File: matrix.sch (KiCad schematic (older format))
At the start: 285 parts, among them SW2 SW_SPDT, SW3 SW_SPDT

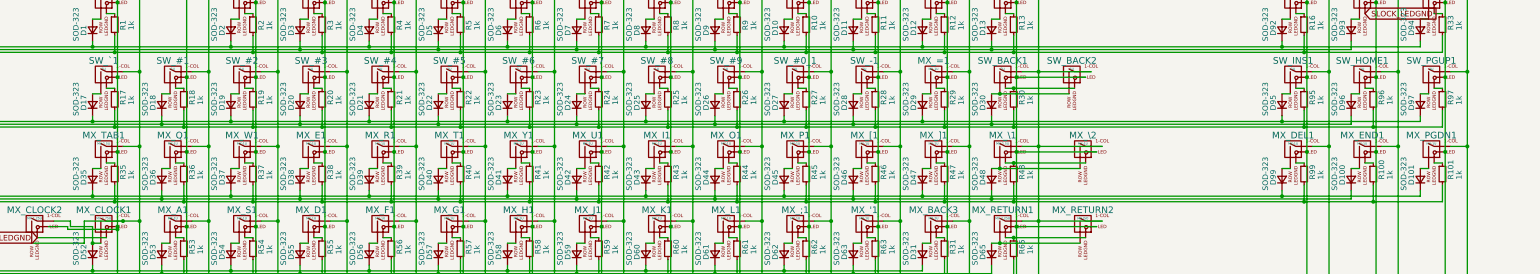
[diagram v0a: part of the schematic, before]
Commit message: Additional row footprint update
Update of a row of footprints from MX only to Alps compatible.
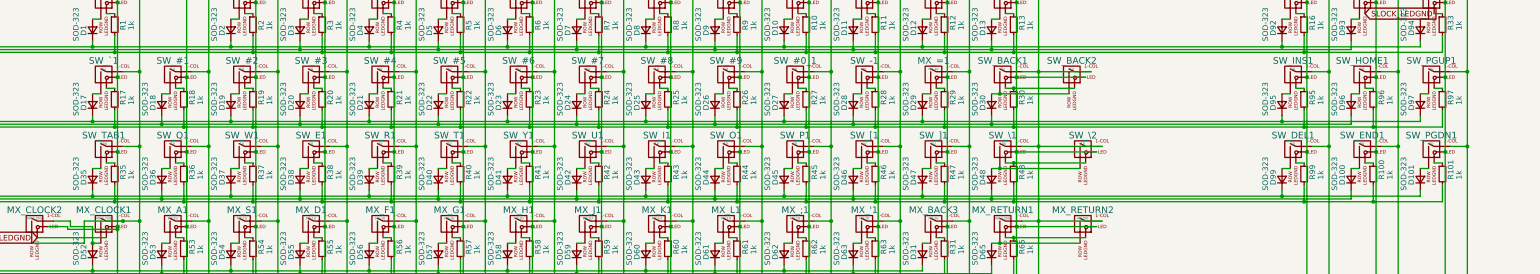
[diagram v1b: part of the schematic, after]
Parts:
- SW_DEL1: renamed from MX_DEL1; value MX-1U -> 1U; footprint MX_Alps_Hybrid:MXOnly-1U -> MX_Alps_Hybrid:MX-1U
- SW_E1: renamed from MX_E1; value MX-1U -> 1U; footprint MX_Alps_Hybrid:MXOnly-1U -> MX_Alps_Hybrid:MX-1U
- SW_END1: renamed from MX_END1; value MX-1U -> 1U; footprint MX_Alps_Hybrid:MXOnly-1U -> MX_Alps_Hybrid:MX-1U
- SW_I1: renamed from MX_I1; value MX-1U -> 1U; footprint MX_Alps_Hybrid:MXOnly-1U -> MX_Alps_Hybrid:MX-1U
- SW_O1: renamed from MX_O1; value MX-1U -> 1U; footprint MX_Alps_Hybrid:MXOnly-1U -> MX_Alps_Hybrid:MX-1U
- SW_P1: renamed from MX_P1; value MX-1U -> 1U; footprint MX_Alps_Hybrid:MXOnly-1U -> MX_Alps_Hybrid:MX-1U
- SW_PGDN1: renamed from MX_PGDN1; value MX-1U -> 1U; footprint MX_Alps_Hybrid:MXOnly-1U -> MX_Alps_Hybrid:MX-1U
- SW_Q1: renamed from MX_Q1; value MX-1U -> 1U; footprint MX_Alps_Hybrid:MXOnly-1U -> MX_Alps_Hybrid:MX-1U
- SW_R1: renamed from MX_R1; value MX-1U -> 1U; footprint MX_Alps_Hybrid:MXOnly-1U -> MX_Alps_Hybrid:MX-1U
- SW_T1: renamed from MX_T1; value MX-1U -> 1U; footprint MX_Alps_Hybrid:MXOnly-1U -> MX_Alps_Hybrid:MX-1U
- SW_TAB1: renamed from MX_TAB1; value MX-1.5U -> 1.5U; footprint MX_Alps_Hybrid:MXOnly-1.5U -> MX_Alps_Hybrid:MX-1.5U
- SW_U1: renamed from MX_U1; value MX-1U -> 1U; footprint MX_Alps_Hybrid:MXOnly-1U -> MX_Alps_Hybrid:MX-1U
- SW_W1: renamed from MX_W1; value MX-1U -> 1U; footprint MX_Alps_Hybrid:MXOnly-1U -> MX_Alps_Hybrid:MX-1U
- SW_Y1: renamed from MX_Y1; value MX-1U -> 1U; footprint MX_Alps_Hybrid:MXOnly-1U -> MX_Alps_Hybrid:MX-1U
- SW_[1: renamed from MX_[1; value MX-1U -> 1U; footprint MX_Alps_Hybrid:MXOnly-1U -> MX_Alps_Hybrid:MX-1U
- SW_\1: renamed from MX_\1; value MX-1.5U -> 1.5U; footprint MX_Alps_Hybrid:MXOnly-1.5U -> MX_Alps_Hybrid:MX-1.5U
- SW_\2: renamed from MX_\2; value MX-1U -> 1U; footprint MX_Alps_Hybrid:MXOnly-1U -> MX_Alps_Hybrid:MX-1U
- SW_]1: renamed from MX_]1; value MX-1U -> 1U; footprint MX_Alps_Hybrid:MXOnly-1U -> MX_Alps_Hybrid:MX-1U
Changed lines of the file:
@@
 $EndComp
 $Comp
-L MX_Alps_Hybrids:MX-1.5U MX_TAB1
+L MX_Alps_Hybrids:MX-1.5U SW_TAB1
 U 1 1 5A2ED339
 P 4825 4100
-F 0 "MX_TAB1" H 4825 4225 60  0000 C CNN
-F 1 "MX-1.5U" H 4825 4150 20  0000 C CNN
-F 2 "MX_Alps_Hybrid:MXOnly-1.5U" H 4800 4075 60  0001 C CNN
+F 0 "SW_TAB1" H 4825 4225 60  0000 C CNN
+F 1 "1.5U" H 4825 4150 20  0000 C CNN
+F 2 "MX_Alps_Hybrid:MX-1.5U" H 4800 4075 60  0001 C CNN
 F 3 "" H 4800 4075 60  0001 C CNN
 	1    4825 4100
@@
 $EndComp
 $Comp
-L MX_Alps_Hybrids:MX-1U MX_Q1
+L MX_Alps_Hybrids:MX-1U SW_Q1
 U 1 1 5A2ED361
 P 5450 4100
-F 0 "MX_Q1" H 5450 4225 60  0000 C CNN
-F 1 "MX-1U" H 5450 4150 20  0000 C CNN
-F 2 "MX_Alps_Hybrid:MXOnly-1U" H 5425 4075 60  0001 C CNN
+F 0 "SW_Q1" H 5450 4225 60  0000 C CNN
+F 1 "1U" H 5450 4150 20  0000 C CNN
+F 2 "MX_Alps_Hybrid:MX-1U" H 5425 4075 60  0001 C CNN
 F 3 "" H 5425 4075 60  0001 C CNN
 	1    5450 4100
@@
 $EndComp
 $Comp
-L MX_Alps_Hybrids:MX-1U MX_W1
+L MX_Alps_Hybrids:MX-1U SW_W1
 U 1 1 5A2ED375
 P 6075 4100
-F 0 "MX_W1" H 6075 4225 60  0000 C CNN
-F 1 "MX-1U" H 6075 4150 20  0000 C CNN
-F 2 "MX_Alps_Hybrid:MXOnly-1U" H 6050 4075 60  0001 C CNN
+F 0 "SW_W1" H 6075 4225 60  0000 C CNN
+F 1 "1U" H 6075 4150 20  0000 C CNN
+F 2 "MX_Alps_Hybrid:MX-1U" H 6050 4075 60  0001 C CNN
 F 3 "" H 6050 4075 60  0001 C CNN
 	1    6075 4100
@@
 $EndComp
 $Comp
-L MX_Alps_Hybrids:MX-1U MX_E1
+L MX_Alps_Hybrids:MX-1U SW_E1
 U 1 1 5A2ED389
 P 6700 4100
-F 0 "MX_E1" H 6700 4225 60  0000 C CNN
-F 1 "MX-1U" H 6700 4150 20  0000 C CNN
-F 2 "MX_Alps_Hybrid:MXOnly-1U" H 6675 4075 60  0001 C CNN
+F 0 "SW_E1" H 6700 4225 60  0000 C CNN
+F 1 "1U" H 6700 4150 20  0000 C CNN
+F 2 "MX_Alps_Hybrid:MX-1U" H 6675 4075 60  0001 C CNN
 F 3 "" H 6675 4075 60  0001 C CNN
 	1    6700 4100
@@
 $EndComp
 $Comp
-L MX_Alps_Hybrids:MX-1U MX_R1
+L MX_Alps_Hybrids:MX-1U SW_R1
 U 1 1 5A2ED39D
 P 7325 4100
-F 0 "MX_R1" H 7325 4225 60  0000 C CNN
-F 1 "MX-1U" H 7325 4150 20  0000 C CNN
-F 2 "MX_Alps_Hybrid:MXOnly-1U" H 7300 4075 60  0001 C CNN
+F 0 "SW_R1" H 7325 4225 60  0000 C CNN
+F 1 "1U" H 7325 4150 20  0000 C CNN
+F 2 "MX_Alps_Hybrid:MX-1U" H 7300 4075 60  0001 C CNN
 F 3 "" H 7300 4075 60  0001 C CNN
 	1    7325 4100
@@
 $EndComp
 $Comp
-L MX_Alps_Hybrids:MX-1U MX_T1
+L MX_Alps_Hybrids:MX-1U SW_T1
 U 1 1 5A2ED3B1
 P 7950 4100
-F 0 "MX_T1" H 7950 4225 60  0000 C CNN
-F 1 "MX-1U" H 7950 4150 20  0000 C CNN
-F 2 "MX_Alps_Hybrid:MXOnly-1U" H 7925 4075 60  0001 C CNN
+F 0 "SW_T1" H 7950 4225 60  0000 C CNN
+F 1 "1U" H 7950 4150 20  0000 C CNN
+F 2 "MX_Alps_Hybrid:MX-1U" H 7925 4075 60  0001 C CNN
 F 3 "" H 7925 4075 60  0001 C CNN
 	1    7950 4100
@@
 $EndComp
 $Comp
-L MX_Alps_Hybrids:MX-1U MX_Y1
+L MX_Alps_Hybrids:MX-1U SW_Y1
 U 1 1 5A2ED3C5
 P 8575 4100
-F 0 "MX_Y1" H 8575 4225 60  0000 C CNN
-F 1 "MX-1U" H 8575 4150 20  0000 C CNN
-F 2 "MX_Alps_Hybrid:MXOnly-1U" H 8550 4075 60  0001 C CNN
+F 0 "SW_Y1" H 8575 4225 60  0000 C CNN
+F 1 "1U" H 8575 4150 20  0000 C CNN
+F 2 "MX_Alps_Hybrid:MX-1U" H 8550 4075 60  0001 C CNN
 F 3 "" H 8550 4075 60  0001 C CNN
 	1    8575 4100
@@
 $EndComp
 $Comp
-L MX_Alps_Hybrids:MX-1U MX_U1
+L MX_Alps_Hybrids:MX-1U SW_U1
 U 1 1 5A2ED3D9
 P 9200 4100
-F 0 "MX_U1" H 9200 4225 60  0000 C CNN
-F 1 "MX-1U" H 9200 4150 20  0000 C CNN
-F 2 "MX_Alps_Hybrid:MXOnly-1U" H 9175 4075 60  0001 C CNN
+F 0 "SW_U1" H 9200 4225 60  0000 C CNN
+F 1 "1U" H 9200 4150 20  0000 C CNN
+F 2 "MX_Alps_Hybrid:MX-1U" H 9175 4075 60  0001 C CNN
 F 3 "" H 9175 4075 60  0001 C CNN
 	1    9200 4100
@@
 $EndComp
 $Comp
-L MX_Alps_Hybrids:MX-1U MX_I1
+L MX_Alps_Hybrids:MX-1U SW_I1
 U 1 1 5A2ED3ED
 P 9825 4100
-F 0 "MX_I1" H 9825 4225 60  0000 C CNN
-F 1 "MX-1U" H 9825 4150 20  0000 C CNN
-F 2 "MX_Alps_Hybrid:MXOnly-1U" H 9800 4075 60  0001 C CNN
+F 0 "SW_I1" H 9825 4225 60  0000 C CNN
+F 1 "1U" H 9825 4150 20  0000 C CNN
+F 2 "MX_Alps_Hybrid:MX-1U" H 9800 4075 60  0001 C CNN
 F 3 "" H 9800 4075 60  0001 C CNN
 	1    9825 4100
@@
 $EndComp
 $Comp
-L MX_Alps_Hybrids:MX-1U MX_O1
+L MX_Alps_Hybrids:MX-1U SW_O1
 U 1 1 5A2ED401
 P 10450 4100
-F 0 "MX_O1" H 10450 4225 60  0000 C CNN
-F 1 "MX-1U" H 10450 4150 20  0000 C CNN
-F 2 "MX_Alps_Hybrid:MXOnly-1U" H 10425 4075 60  0001 C CNN
+F 0 "SW_O1" H 10450 4225 60  0000 C CNN
+F 1 "1U" H 10450 4150 20  0000 C CNN
+F 2 "MX_Alps_Hybrid:MX-1U" H 10425 4075 60  0001 C CNN
 F 3 "" H 10425 4075 60  0001 C CNN
 	1    10450 4100
@@
 $EndComp
 $Comp
-L MX_Alps_Hybrids:MX-1U MX_P1
+L MX_Alps_Hybrids:MX-1U SW_P1
 U 1 1 5A2ED415
 P 11075 4100
-F 0 "MX_P1" H 11075 4225 60  0000 C CNN
-F 1 "MX-1U" H 11075 4150 20  0000 C CNN
-F 2 "MX_Alps_Hybrid:MXOnly-1U" H 11050 4075 60  0001 C CNN
+F 0 "SW_P1" H 11075 4225 60  0000 C CNN
+F 1 "1U" H 11075 4150 20  0000 C CNN
+F 2 "MX_Alps_Hybrid:MX-1U" H 11050 4075 60  0001 C CNN
 F 3 "" H 11050 4075 60  0001 C CNN
 	1    11075 4100
@@
 $EndComp
 $Comp
-L MX_Alps_Hybrids:MX-1U MX_[1
+L MX_Alps_Hybrids:MX-1U SW_[1
 U 1 1 5A2ED429
 P 11700 4100
-F 0 "MX_[1" H 11700 4225 60  0000 C CNN
-F 1 "MX-1U" H 11700 4150 20  0000 C CNN
-F 2 "MX_Alps_Hybrid:MXOnly-1U" H 11675 4075 60  0001 C CNN
+F 0 "SW_[1" H 11700 4225 60  0000 C CNN
+F 1 "1U" H 11700 4150 20  0000 C CNN
+F 2 "MX_Alps_Hybrid:MX-1U" H 11675 4075 60  0001 C CNN
 F 3 "" H 11675 4075 60  0001 C CNN
 	1    11700 4100
@@
 $EndComp
 $Comp
-L MX_Alps_Hybrids:MX-1U MX_]1
+L MX_Alps_Hybrids:MX-1U SW_]1
 U 1 1 5A2ED43D
 P 12325 4100
-F 0 "MX_]1" H 12325 4225 60  0000 C CNN
-F 1 "MX-1U" H 12325 4150 20  0000 C CNN
-F 2 "MX_Alps_Hybrid:MXOnly-1U" H 12300 4075 60  0001 C CNN
+F 0 "SW_]1" H 12325 4225 60  0000 C CNN
+F 1 "1U" H 12325 4150 20  0000 C CNN
+F 2 "MX_Alps_Hybrid:MX-1U" H 12300 4075 60  0001 C CNN
 F 3 "" H 12300 4075 60  0001 C CNN
 	1    12325 4100
@@
 $EndComp
 $Comp
-L MX_Alps_Hybrids:MX-1.5U MX_\1
+L MX_Alps_Hybrids:MX-1.5U SW_\1
 U 1 1 5A2ED451
 P 12950 4100
-F 0 "MX_\\1" H 12950 4225 60  0000 C CNN
-F 1 "MX-1.5U" H 12950 4150 20  0000 C CNN
-F 2 "MX_Alps_Hybrid:MXOnly-1.5U" H 12925 4075 60  0001 C CNN
+F 0 "SW_\\1" H 12950 4225 60  0000 C CNN
+F 1 "1.5U" H 12950 4150 20  0000 C CNN
+F 2 "MX_Alps_Hybrid:MX-1.5U" H 12925 4075 60  0001 C CNN
 F 3 "" H 12925 4075 60  0001 C CNN
 	1    12950 4100
@@
 Connection ~ 16950 4125
 $Comp
-L MX_Alps_Hybrids:MX-1U MX_PGDN1
+L MX_Alps_Hybrids:MX-1U SW_PGDN1
 U 1 1 5ADCFA54
 P 16825 4100
-F 0 "MX_PGDN1" H 16825 4225 60  0000 C CNN
-F 1 "MX-1U" H 16825 4150 20  0000 C CNN
-F 2 "MX_Alps_Hybrid:MXOnly-1U" H 16800 4075 60  0001 C CNN
+F 0 "SW_PGDN1" H 16825 4225 60  0000 C CNN
+F 1 "1U" H 16825 4150 20  0000 C CNN
+F 2 "MX_Alps_Hybrid:MX-1U" H 16800 4075 60  0001 C CNN
 F 3 "" H 16800 4075 60  0001 C CNN
 	1    16825 4100
@@
 Connection ~ 16325 4125
 $Comp
-L MX_Alps_Hybrids:MX-1U MX_END1
+L MX_Alps_Hybrids:MX-1U SW_END1
 U 1 1 5ADCFA42
 P 16200 4100
-F 0 "MX_END1" H 16200 4225 60  0000 C CNN
-F 1 "MX-1U" H 16200 4150 20  0000 C CNN
-F 2 "MX_Alps_Hybrid:MXOnly-1U" H 16175 4075 60  0001 C CNN
+F 0 "SW_END1" H 16200 4225 60  0000 C CNN
+F 1 "1U" H 16200 4150 20  0000 C CNN
+F 2 "MX_Alps_Hybrid:MX-1U" H 16175 4075 60  0001 C CNN
 F 3 "" H 16175 4075 60  0001 C CNN
 	1    16200 4100
@@
 Connection ~ 15700 4125
 $Comp
-L MX_Alps_Hybrids:MX-1U MX_DEL1
+L MX_Alps_Hybrids:MX-1U SW_DEL1
 U 1 1 5ADCFA30
 P 15575 4100
-F 0 "MX_DEL1" H 15575 4225 60  0000 C CNN
-F 1 "MX-1U" H 15575 4150 20  0000 C CNN
-F 2 "MX_Alps_Hybrid:MXOnly-1U" H 15550 4075 60  0001 C CNN
+F 0 "SW_DEL1" H 15575 4225 60  0000 C CNN
+F 1 "1U" H 15575 4150 20  0000 C CNN
+F 2 "MX_Alps_Hybrid:MX-1U" H 15550 4075 60  0001 C CNN
 F 3 "" H 15550 4075 60  0001 C CNN
 	1    15575 4100
@@
 $EndComp
 $Comp
-L MX_Alps_Hybrids:MX-1U MX_\2
+L MX_Alps_Hybrids:MX-1U SW_\2
 U 1 1 5F322A9F
 P 13675 4100
-F 0 "MX_\\2" H 13675 4225 60  0000 C CNN
-F 1 "MX-1U" H 13675 4150 20  0000 C CNN
-F 2 "MX_Alps_Hybrid:MXOnly-1U" H 13650 4075 60  0001 C CNN
+F 0 "SW_\\2" H 13675 4225 60  0000 C CNN
+F 1 "1U" H 13675 4150 20  0000 C CNN
+F 2 "MX_Alps_Hybrid:MX-1U" H 13650 4075 60  0001 C CNN
 F 3 "" H 13650 4075 60  0001 C CNN
 	1    13675 4100

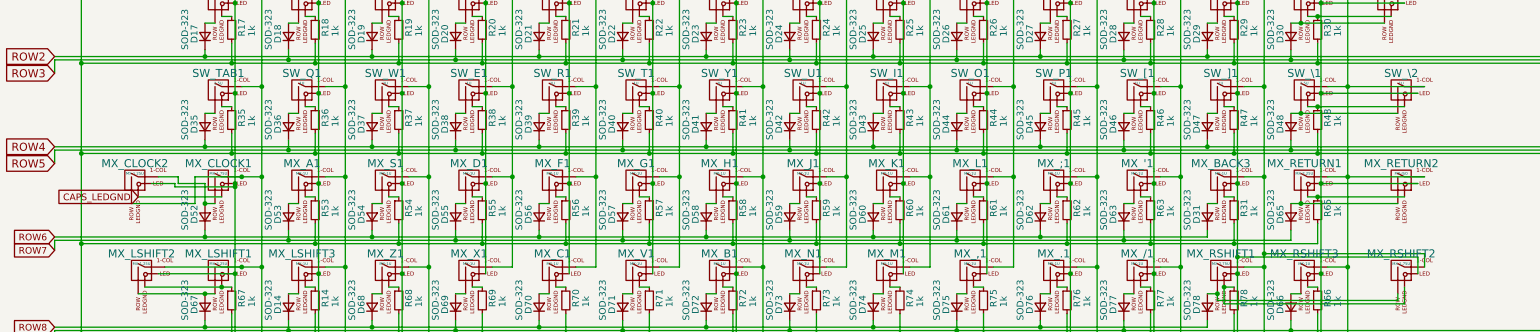
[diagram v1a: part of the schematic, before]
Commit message: Additional row of footprint updates
Enter row footprints updated to Alps compatible.
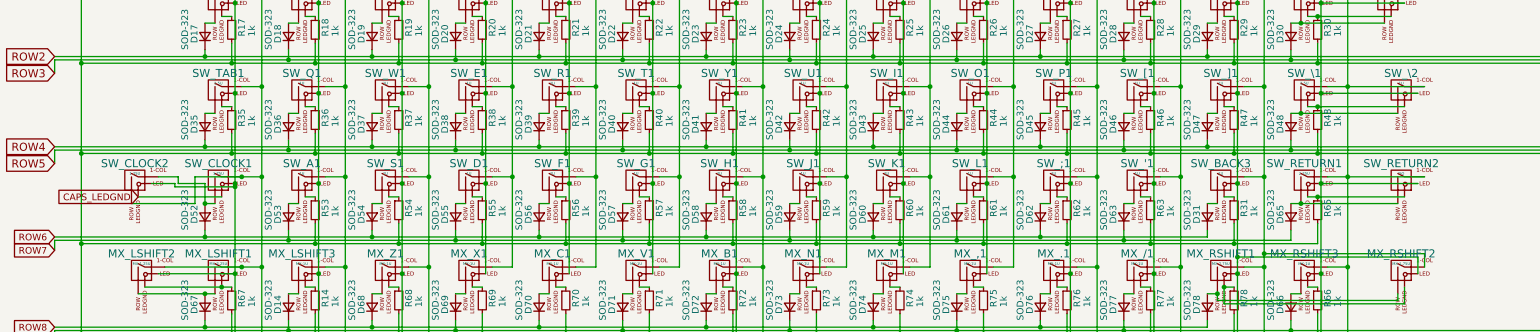
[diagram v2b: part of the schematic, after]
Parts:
- SW_'1: renamed from MX_'1; value MX-1U -> 1U; footprint MX_Alps_Hybrid:MXOnly-1U -> MX_Alps_Hybrid:MX-1U
- SW_;1: renamed from MX_;1; value MX-1U -> 1U; footprint MX_Alps_Hybrid:MXOnly-1U -> MX_Alps_Hybrid:MX-1U
- SW_A1: renamed from MX_A1; value MX-1U -> 1U; footprint MX_Alps_Hybrid:MXOnly-1U -> MX_Alps_Hybrid:MX-1U
- SW_BACK3: renamed from MX_BACK3; value MX-1U -> 1U; footprint MX_Alps_Hybrid:MXOnly-1U -> MX_Alps_Hybrid:MX-1U
- SW_CLOCK1: renamed from MX_CLOCK1; value MX-1.75U -> 1.75U; footprint MX_Alps_Hybrid:MXOnly-1.75U -> MX_Alps_Hybrid:MX-1.75U
- SW_CLOCK2: renamed from MX_CLOCK2; value MX-1.25U -> 1.25U; footprint MX_Alps_Hybrid:MXOnly-1.25U-FLIPPED -> MX_Alps_Hybrid:MX-1.25U-FLIPPED
- SW_D1: renamed from MX_D1; value MX-1U -> 1U; footprint MX_Alps_Hybrid:MXOnly-1U -> MX_Alps_Hybrid:MX-1U
- SW_F1: renamed from MX_F1; value MX-1U -> 1U; footprint MX_Alps_Hybrid:MXOnly-1U -> MX_Alps_Hybrid:MX-1U
- SW_G1: renamed from MX_G1; value MX-1U -> 1U; footprint MX_Alps_Hybrid:MXOnly-1U -> MX_Alps_Hybrid:MX-1U
- SW_H1: renamed from MX_H1; value MX-1U -> 1U; footprint MX_Alps_Hybrid:MXOnly-1U -> MX_Alps_Hybrid:MX-1U
- SW_J1: renamed from MX_J1; value MX-1U -> 1U; footprint MX_Alps_Hybrid:MXOnly-1U -> MX_Alps_Hybrid:MX-1U
- SW_K1: renamed from MX_K1; value MX-1U -> 1U; footprint MX_Alps_Hybrid:MXOnly-1U -> MX_Alps_Hybrid:MX-1U
- SW_L1: renamed from MX_L1; value MX-1U -> 1U; footprint MX_Alps_Hybrid:MXOnly-1U -> MX_Alps_Hybrid:MX-1U
- SW_RETURN1: renamed from MX_RETURN1; value MX-2.25U -> 2.25U; footprint MX_Alps_Hybrid:MXOnly-2.25U -> MX_Alps_Hybrid:MX-2.25U
- SW_RETURN2: renamed from MX_RETURN2; value MX-ISO -> ISO; footprint MX_Alps_Hybrid:MXOnly-ISO-ROTATED-ReversedStabilizers -> MX_Alps_Hybrid:MX-ISO-ReversedStabilizers
- SW_S1: renamed from MX_S1; value MX-1U -> 1U; footprint MX_Alps_Hybrid:MXOnly-1U -> MX_Alps_Hybrid:MX-1U
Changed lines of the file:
@@
 $EndComp
 $Comp
-L MX_Alps_Hybrids:MX-1.75U MX_CLOCK1
+L MX_Alps_Hybrids:MX-1.75U SW_CLOCK1
 U 1 1 5A2ED4A1
 P 4825 4775
-F 0 "MX_CLOCK1" H 4825 4900 60  0000 C CNN
-F 1 "MX-1.75U" H 4825 4825 20  0000 C CNN
-F 2 "MX_Alps_Hybrid:MXOnly-1.75U" H 4800 4750 60  0001 C CNN
+F 0 "SW_CLOCK1" H 4825 4900 60  0000 C CNN
+F 1 "1.75U" H 4825 4825 20  0000 C CNN
+F 2 "MX_Alps_Hybrid:MX-1.75U" H 4800 4750 60  0001 C CNN
 F 3 "" H 4800 4750 60  0001 C CNN
 	1    4825 4775
@@
 $EndComp
 $Comp
-L MX_Alps_Hybrids:MX-1U MX_A1
+L MX_Alps_Hybrids:MX-1U SW_A1
 U 1 1 5A2ED4C9
 P 5450 4775
-F 0 "MX_A1" H 5450 4900 60  0000 C CNN
-F 1 "MX-1U" H 5450 4825 20  0000 C CNN
-F 2 "MX_Alps_Hybrid:MXOnly-1U" H 5425 4750 60  0001 C CNN
+F 0 "SW_A1" H 5450 4900 60  0000 C CNN
+F 1 "1U" H 5450 4825 20  0000 C CNN
+F 2 "MX_Alps_Hybrid:MX-1U" H 5425 4750 60  0001 C CNN
 F 3 "" H 5425 4750 60  0001 C CNN
 	1    5450 4775
@@
 $EndComp
 $Comp
-L MX_Alps_Hybrids:MX-1U MX_S1
+L MX_Alps_Hybrids:MX-1U SW_S1
 U 1 1 5A2ED4DD
 P 6075 4775
-F 0 "MX_S1" H 6075 4900 60  0000 C CNN
-F 1 "MX-1U" H 6075 4825 20  0000 C CNN
-F 2 "MX_Alps_Hybrid:MXOnly-1U" H 6050 4750 60  0001 C CNN
+F 0 "SW_S1" H 6075 4900 60  0000 C CNN
+F 1 "1U" H 6075 4825 20  0000 C CNN
+F 2 "MX_Alps_Hybrid:MX-1U" H 6050 4750 60  0001 C CNN
 F 3 "" H 6050 4750 60  0001 C CNN
 	1    6075 4775
@@
 $EndComp
 $Comp
-L MX_Alps_Hybrids:MX-1U MX_D1
+L MX_Alps_Hybrids:MX-1U SW_D1
 U 1 1 5A2ED4F1
 P 6700 4775
-F 0 "MX_D1" H 6700 4900 60  0000 C CNN
-F 1 "MX-1U" H 6700 4825 20  0000 C CNN
-F 2 "MX_Alps_Hybrid:MXOnly-1U" H 6675 4750 60  0001 C CNN
+F 0 "SW_D1" H 6700 4900 60  0000 C CNN
+F 1 "1U" H 6700 4825 20  0000 C CNN
+F 2 "MX_Alps_Hybrid:MX-1U" H 6675 4750 60  0001 C CNN
 F 3 "" H 6675 4750 60  0001 C CNN
 	1    6700 4775
@@
 $EndComp
 $Comp
-L MX_Alps_Hybrids:MX-1U MX_F1
+L MX_Alps_Hybrids:MX-1U SW_F1
 U 1 1 5A2ED505
 P 7325 4775
-F 0 "MX_F1" H 7325 4900 60  0000 C CNN
-F 1 "MX-1U" H 7325 4825 20  0000 C CNN
-F 2 "MX_Alps_Hybrid:MXOnly-1U" H 7300 4750 60  0001 C CNN
+F 0 "SW_F1" H 7325 4900 60  0000 C CNN
+F 1 "1U" H 7325 4825 20  0000 C CNN
+F 2 "MX_Alps_Hybrid:MX-1U" H 7300 4750 60  0001 C CNN
 F 3 "" H 7300 4750 60  0001 C CNN
 	1    7325 4775
@@
 $EndComp
 $Comp
-L MX_Alps_Hybrids:MX-1U MX_G1
+L MX_Alps_Hybrids:MX-1U SW_G1
 U 1 1 5A2ED519
 P 7950 4775
-F 0 "MX_G1" H 7950 4900 60  0000 C CNN
-F 1 "MX-1U" H 7950 4825 20  0000 C CNN
-F 2 "MX_Alps_Hybrid:MXOnly-1U" H 7925 4750 60  0001 C CNN
+F 0 "SW_G1" H 7950 4900 60  0000 C CNN
+F 1 "1U" H 7950 4825 20  0000 C CNN
+F 2 "MX_Alps_Hybrid:MX-1U" H 7925 4750 60  0001 C CNN
 F 3 "" H 7925 4750 60  0001 C CNN
 	1    7950 4775
@@
 $EndComp
 $Comp
-L MX_Alps_Hybrids:MX-1U MX_H1
+L MX_Alps_Hybrids:MX-1U SW_H1
 U 1 1 5A2ED52D
 P 8575 4775
-F 0 "MX_H1" H 8575 4900 60  0000 C CNN
-F 1 "MX-1U" H 8575 4825 20  0000 C CNN
-F 2 "MX_Alps_Hybrid:MXOnly-1U" H 8550 4750 60  0001 C CNN
+F 0 "SW_H1" H 8575 4900 60  0000 C CNN
+F 1 "1U" H 8575 4825 20  0000 C CNN
+F 2 "MX_Alps_Hybrid:MX-1U" H 8550 4750 60  0001 C CNN
 F 3 "" H 8550 4750 60  0001 C CNN
 	1    8575 4775
@@
 $EndComp
 $Comp
-L MX_Alps_Hybrids:MX-1U MX_J1
+L MX_Alps_Hybrids:MX-1U SW_J1
 U 1 1 5A2ED541
 P 9200 4775
-F 0 "MX_J1" H 9200 4900 60  0000 C CNN
-F 1 "MX-1U" H 9200 4825 20  0000 C CNN
-F 2 "MX_Alps_Hybrid:MXOnly-1U" H 9175 4750 60  0001 C CNN
+F 0 "SW_J1" H 9200 4900 60  0000 C CNN
+F 1 "1U" H 9200 4825 20  0000 C CNN
+F 2 "MX_Alps_Hybrid:MX-1U" H 9175 4750 60  0001 C CNN
 F 3 "" H 9175 4750 60  0001 C CNN
 	1    9200 4775
@@
 $EndComp
 $Comp
-L MX_Alps_Hybrids:MX-1U MX_K1
+L MX_Alps_Hybrids:MX-1U SW_K1
 U 1 1 5A2ED555
 P 9825 4775
-F 0 "MX_K1" H 9825 4900 60  0000 C CNN
-F 1 "MX-1U" H 9825 4825 20  0000 C CNN
-F 2 "MX_Alps_Hybrid:MXOnly-1U" H 9800 4750 60  0001 C CNN
+F 0 "SW_K1" H 9825 4900 60  0000 C CNN
+F 1 "1U" H 9825 4825 20  0000 C CNN
+F 2 "MX_Alps_Hybrid:MX-1U" H 9800 4750 60  0001 C CNN
 F 3 "" H 9800 4750 60  0001 C CNN
 	1    9825 4775
@@
 $EndComp
 $Comp
-L MX_Alps_Hybrids:MX-1U MX_L1
+L MX_Alps_Hybrids:MX-1U SW_L1
 U 1 1 5A2ED569
 P 10450 4775
-F 0 "MX_L1" H 10450 4900 60  0000 C CNN
-F 1 "MX-1U" H 10450 4825 20  0000 C CNN
-F 2 "MX_Alps_Hybrid:MXOnly-1U" H 10425 4750 60  0001 C CNN
+F 0 "SW_L1" H 10450 4900 60  0000 C CNN
+F 1 "1U" H 10450 4825 20  0000 C CNN
+F 2 "MX_Alps_Hybrid:MX-1U" H 10425 4750 60  0001 C CNN
 F 3 "" H 10425 4750 60  0001 C CNN
 	1    10450 4775
@@
 $EndComp
 $Comp
-L MX_Alps_Hybrids:MX-1U MX_;1
+L MX_Alps_Hybrids:MX-1U SW_;1
 U 1 1 5A2ED57D
 P 11075 4775
-F 0 "MX_;1" H 11075 4900 60  0000 C CNN
-F 1 "MX-1U" H 11075 4825 20  0000 C CNN
-F 2 "MX_Alps_Hybrid:MXOnly-1U" H 11050 4750 60  0001 C CNN
+F 0 "SW_;1" H 11075 4900 60  0000 C CNN
+F 1 "1U" H 11075 4825 20  0000 C CNN
+F 2 "MX_Alps_Hybrid:MX-1U" H 11050 4750 60  0001 C CNN
 F 3 "" H 11050 4750 60  0001 C CNN
 	1    11075 4775
@@
 $EndComp
 $Comp
-L MX_Alps_Hybrids:MX-1U MX_'1
+L MX_Alps_Hybrids:MX-1U SW_'1
 U 1 1 5A2ED591
 P 11700 4775
-F 0 "MX_'1" H 11700 4900 60  0000 C CNN
-F 1 "MX-1U" H 11700 4825 20  0000 C CNN
-F 2 "MX_Alps_Hybrid:MXOnly-1U" H 11675 4750 60  0001 C CNN
+F 0 "SW_'1" H 11700 4900 60  0000 C CNN
+F 1 "1U" H 11700 4825 20  0000 C CNN
+F 2 "MX_Alps_Hybrid:MX-1U" H 11675 4750 60  0001 C CNN
 F 3 "" H 11675 4750 60  0001 C CNN
 	1    11700 4775
@@
 $EndComp
 $Comp
-L MX_Alps_Hybrids:MX-1.25U MX_CLOCK2
+L MX_Alps_Hybrids:MX-1.25U SW_CLOCK2
 U 1 1 5A2ED4B5
 P 4200 4775
-F 0 "MX_CLOCK2" H 4200 4900 60  0000 C CNN
-F 1 "MX-1.25U" H 4200 4825 20  0000 C CNN
-F 2 "MX_Alps_Hybrid:MXOnly-1.25U-FLIPPED" H 4175 4750 60  0001 C CNN
+F 0 "SW_CLOCK2" H 4200 4900 60  0000 C CNN
+F 1 "1.25U" H 4200 4825 20  0000 C CNN
+F 2 "MX_Alps_Hybrid:MX-1.25U-FLIPPED" H 4175 4750 60  0001 C CNN
 F 3 "" H 4175 4750 60  0001 C CNN
 	1    4200 4775
@@
 $EndComp
 $Comp
-L MX_Alps_Hybrids:MX-1U MX_BACK3
+L MX_Alps_Hybrids:MX-1U SW_BACK3
 U 1 1 5A30E826
 P 12325 4775
-F 0 "MX_BACK3" H 12325 4900 60  0000 C CNN
-F 1 "MX-1U" H 12325 4825 20  0000 C CNN
-F 2 "MX_Alps_Hybrid:MXOnly-1U" H 12300 4750 60  0001 C CNN
+F 0 "SW_BACK3" H 12325 4900 60  0000 C CNN
+F 1 "1U" H 12325 4825 20  0000 C CNN
+F 2 "MX_Alps_Hybrid:MX-1U" H 12300 4750 60  0001 C CNN
 F 3 "" H 12300 4750 60  0001 C CNN
 	1    12325 4775
@@
 $EndComp
 $Comp
-L MX_Alps_Hybrids:MX-2.25U MX_RETURN1
+L MX_Alps_Hybrids:MX-2.25U SW_RETURN1
 U 1 1 5A321A08
 P 12950 4775
-F 0 "MX_RETURN1" H 12950 4900 60  0000 C CNN
-F 1 "MX-2.25U" H 12950 4825 20  0000 C CNN
-F 2 "MX_Alps_Hybrid:MXOnly-2.25U" H 12925 4750 60  0001 C CNN
+F 0 "SW_RETURN1" H 12950 4900 60  0000 C CNN
+F 1 "2.25U" H 12950 4825 20  0000 C CNN
+F 2 "MX_Alps_Hybrid:MX-2.25U" H 12925 4750 60  0001 C CNN
 F 3 "" H 12925 4750 60  0001 C CNN
 	1    12950 4775
@@
 $EndComp
 $Comp
-L MX_Alps_Hybrids:MX-2.25U MX_RETURN2
+L MX_Alps_Hybrids:MX-2.25U SW_RETURN2
 U 1 1 5F32342D
 P 13675 4775
-F 0 "MX_RETURN2" H 13675 4900 60  0000 C CNN
-F 1 "MX-ISO" H 13675 4825 20  0000 C CNN
-F 2 "MX_Alps_Hybrid:MXOnly-ISO-ROTATED-ReversedStabilizers" H 13650 4750 60  0001 C CNN
+F 0 "SW_RETURN2" H 13675 4900 60  0000 C CNN
+F 1 "ISO" H 13675 4825 20  0000 C CNN
+F 2 "MX_Alps_Hybrid:MX-ISO-ReversedStabilizers" H 13650 4750 60  0001 C CNN
 F 3 "" H 13650 4750 60  0001 C CNN
 	1    13675 4775
